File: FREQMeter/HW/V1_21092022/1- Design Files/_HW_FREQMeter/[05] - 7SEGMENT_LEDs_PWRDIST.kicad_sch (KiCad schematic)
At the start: 0 parts

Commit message: progress on Frequency meter hardware
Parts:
- added C? (x4): 100nF, symbol FREQMeter:100nF
- added D? (x6): LED_RED, symbol FREQMeter:LED_RED
- added DIS?: LDQ-M282RI, symbol FREQMeter:LDQ-M282RI
- added R? (x6): 10KR, symbol FREQMeter:10KR
- added U? (x3): 74HC595BQ,115, symbol FREQMeter:74HC595BQ,115
- added U? (x2): 1KR_ARR_8, symbol FREQMeter:1KR_ARR_8
- added U?: 74LVC3G34GS,115, symbol FREQMeter:74LVC3G34GS,115
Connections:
- new net: R?.2, U?.10 (~{MR}) (x3)
- new net: R?.2, U?.13 (~{OE}) (x3)
- new net: U?.1 (Q1), U?.2 (x2)
- new net: U?.1, U?.15 (Q0) (x2)
- new net: U?.2 (Q2), U?.3 (x2)
- new net: U?.3 (Q3), U?.4 (x2)
- new net: U?.4 (Q4), U?.5 (x2)
- new net: U?.5 (Q5), U?.6 (x2)
- new net: U?.6 (Q6), U?.7
- new net: U?.7 (Q7), U?.8
- new net: U?.1 (1A), U?.4 (Q4)
- new net: U?.3 (2A), U?.5 (Q5)
- new net: U?.6 (3A), U?.6 (Q6)
- new net DIGIT_1: DIS?.12 (DIG_1), U?.15 (Q0)
- new net DIGIT_2: DIS?.9 (DIG_2), U?.1 (Q1)
- new net DIGIT_3: DIS?.8 (DIG_3), U?.2 (Q2)
- new net DIGIT_4: DIS?.6 (DIG_4), U?.3 (Q3)
- new net DIS_FREQ: D?.2, U?.16
- new net DIS_PULSE: D?.2, U?.14
- new net DIS_RPM: D?.2, U?.15
- new net DIS_X1000: D?.2, U?.13
- new net DIS_X1000000: D?.2, U?.12
- new net DIS_X1000000000: D?.2, U?.11
- new net GND: C?.1, C?.1, C?.1, C?.1, R?.1, R?.1, R?.1, U?.4 (GND), U?.Q8 (GND), U?.Q8 (GND), U?.Q8 (GND)
- new net SEG_A: DIS?.11 (A), U?.16
- new net SEG_B: DIS?.7 (B), U?.15
- new net SEG_C: DIS?.4 (C), U?.14
- new net SEG_D: DIS?.2 (D), U?.13
- new net SEG_DP: DIS?.3 (DP1), U?.9
- new net SEG_E: DIS?.1 (E), U?.12
- new net SEG_F: DIS?.10 (F), U?.11
- new net SEG_G: DIS?.5 (G), U?.10
- new net SR_7SEG_DATA: U?.14 (DS)
- new net SR_LED_DATA: U?.14 (DS), U?.9 (Q7S)
- new net SR_PWR_DATA: U?.14 (DS), U?.9 (Q7S)
- new net SR_SCHP_CLK: U?.11 (SCHP), U?.11 (SCHP), U?.11 (SCHP)
- new net SR_STCP_CLK: U?.12 (STCP), U?.12 (STCP), U?.12 (STCP)
- new net VCC: C?.2, C?.2, C?.2, C?.2, D?.1, D?.1, D?.1, D?.1, D?.1, D?.1, R?.1, R?.1, R?.1, U?.16 (VCC), U?.16 (VCC), U?.16 (VCC), U?.8 (VCC)
- new net X1000000000_PWR: U?.2 (3Y)
- new net X1000000_PWR: U?.5 (2Y)
- new net X1000_PWR: U?.7 (1Y)

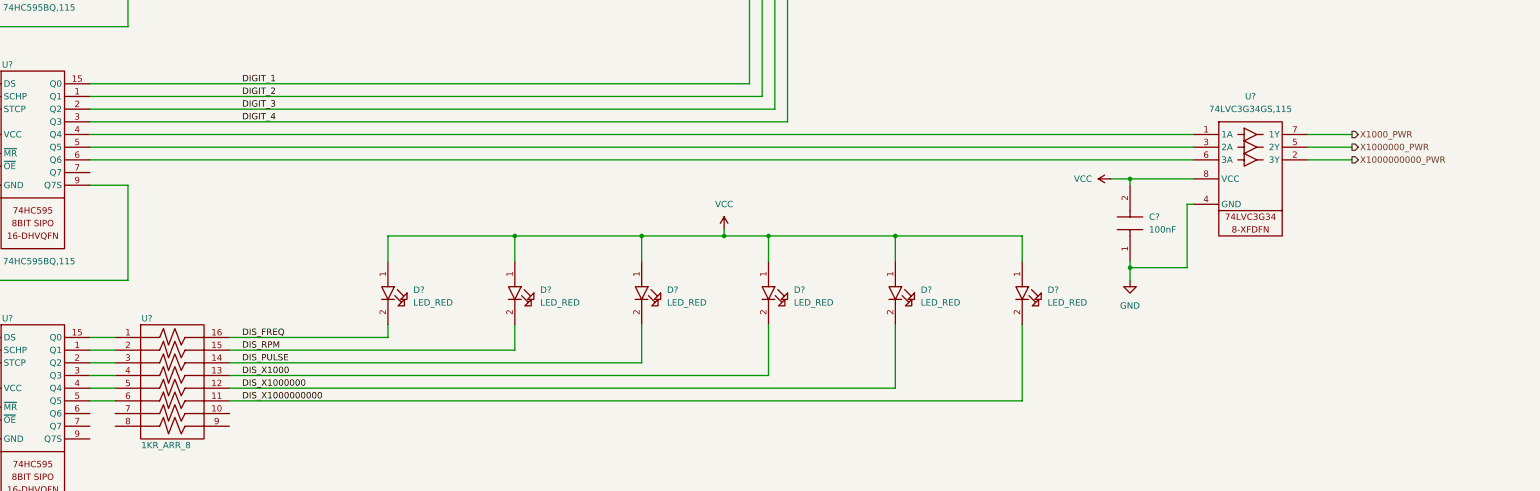
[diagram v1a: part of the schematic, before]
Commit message: frequency meter input schematic in progress
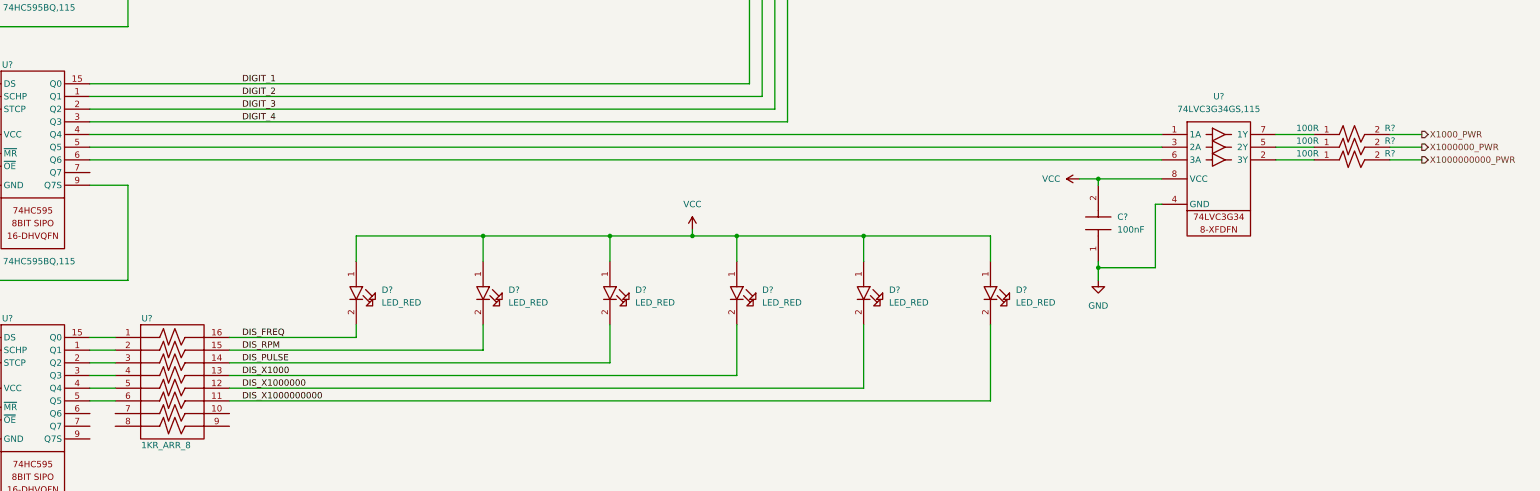
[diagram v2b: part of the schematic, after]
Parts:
- added R? (x3): 100R, symbol FREQMeter:100R
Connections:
- net X1000000000_PWR: now also R?.2; no longer U?.2 (3Y)
- net X1000000_PWR: now also R?.2; no longer U?.5 (2Y)
- net X1000_PWR: now also R?.2; no longer U?.7 (1Y)
- new net: R?.1, U?.7 (1Y)
- new net: R?.1, U?.2 (3Y)
- new net: R?.1, U?.5 (2Y)
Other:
- moved on the sheet: C?, D?, U?
